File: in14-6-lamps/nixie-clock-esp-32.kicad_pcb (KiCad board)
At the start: 2 copper layers, 153 x 50 mm, 90 parts, among them J1 Conn_01x02_Pin, J2 Conn_01x02_Pin, J3 Conn_01x06_Pin, J4 Conn_01x02_Pin, Q1 MMBTA42, Q10 2N7002, Q11 MMBTA42, Q12 MMBTA92, Q13 MMBTA42, Q14 MMBTA92, Q15 MMBTA42, Q2 MMBTA92, Q3 MMBTA42, Q4 MMBTA92, Q5 MMBTA42, Q6 MMBTA92, Q7 MMBTA42, Q8 MMBTA92, Q9 MMBTA42, SW1 SW_Push, U1 max688 boost regulator 5 to 1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, U2 AMS1117-3.3, U3 ESP32-WROOM-32D, U4 DS3231M, U5 74141

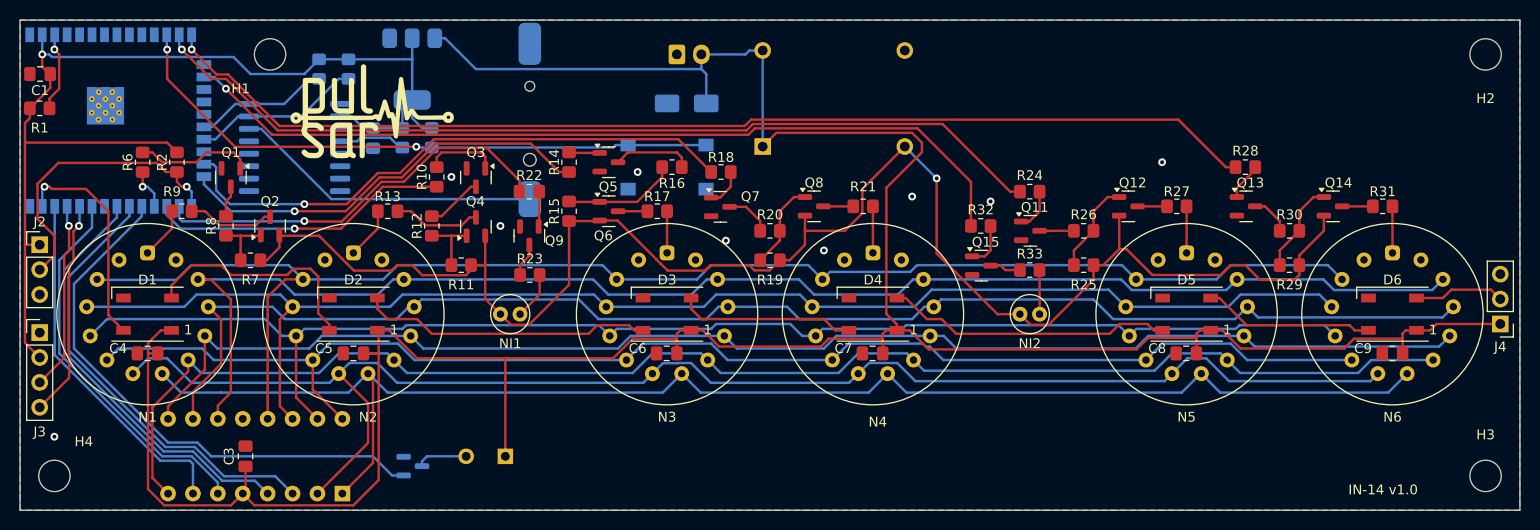
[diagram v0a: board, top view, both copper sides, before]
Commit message: fix i2c connection
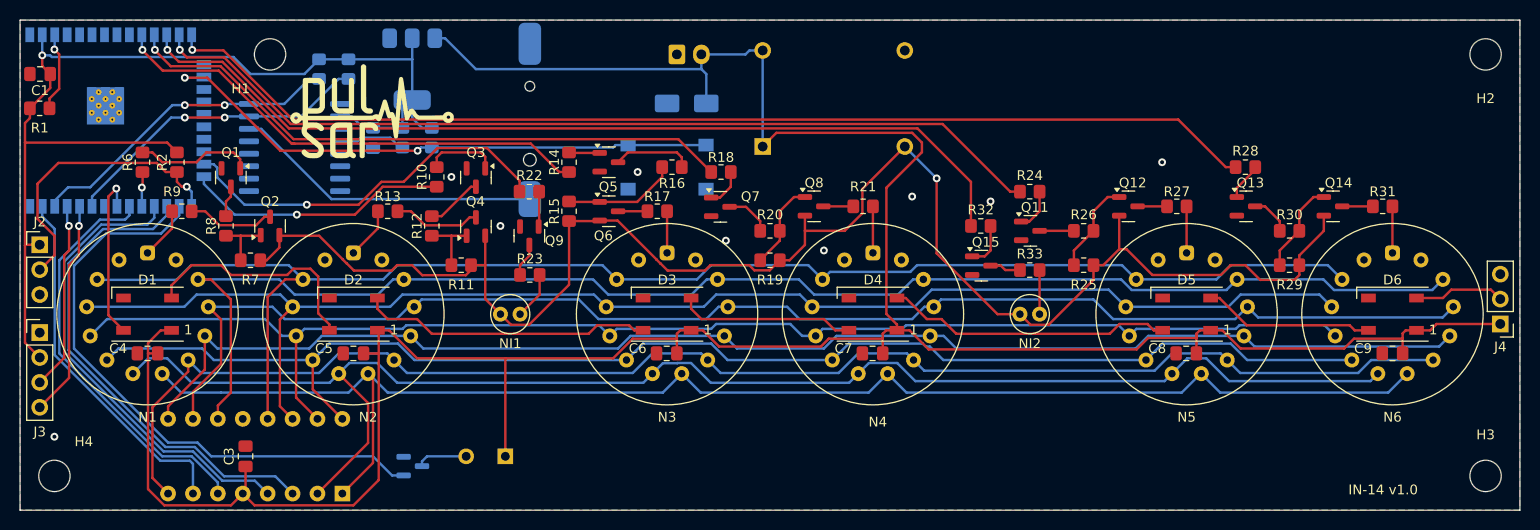
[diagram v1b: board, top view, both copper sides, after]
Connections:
- U3 pad 10: unconnected-(U3-IO25-Pad10) -> A3
- U3 pad 11: unconnected-(U3-IO26-Pad11) -> A4
- U3 pad 12: /control/BTN2 -> IN2
- U3 pad 16: IN2 -> /control/BTN2
- U3 pad 20: /control/SCK -> unconnected-(U3-SCK/CLK-Pad20)
- U3 pad 21: /control/SDA -> unconnected-(U3-SDO/SD0-Pad21)
- U3 pad 23: A4 -> IN1
- U3 pad 24: A3 -> A2
- U3 pad 26: IN1 -> /control/BUZZ
- U3 pad 27: A2 -> DEC0
- U3 pad 28: A1 -> DEC3
- U3 pad 29: /control/BUZZ -> A1
- U3 pad 30: DEC0 -> DEC1
- U3 pad 31: DEC3 -> WS2812
- U3 pad 33: DEC1 -> /control/SDA
- U3 pad 36: DEC2 -> /control/SCK
- U3 pad 37: WS2812 -> DEC2
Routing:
- net /control/SCK: track 13.8 -> 32.8 mm, vias 0 -> 2
- net /control/SDA: track 17.3 -> 32.2 mm, vias 0 -> 2
- net A3: track 43.2 -> 50.5 mm
- net IN2: track 87.7 -> 93.6 mm
- net WS2812: track 22.4 -> 17.3 mm
- net /control/BUZZ: track 56.5 -> 61.2 mm
- net DEC0: track 46.1 -> 50.7 mm
- net A4: track 59.0 -> 63.5 mm
- net DEC3: track 43.8 -> 48.2 mm
- net /control/BTN2: track 62.5 -> 58.5 mm
- net A2: track 30.8 -> 27.0 mm
- net DEC1: track 39.1 -> 42.2 mm
- net IN1: track 41.7 -> 39.4 mm
- net A1: track 4.29 -> 3.53 mm
- net A6: track 113.5 -> 113.0 mm
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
